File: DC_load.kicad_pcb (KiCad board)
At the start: 2 copper layers, 110 x 145 mm, 103 parts, among them J1 Conn_Coaxial, J2 red_terminal, J3 4 mm terminal, J4 4 mm terminal, J5 black terminal, J6 USB_B, Q3 FQP19N20C, Q4 FQP19N20C, Q5 FQP19N20C, Q6 FQP19N20C, SW1 RotaryEncoder_Switch, SW2 RotaryEncoder_Switch, U1 FSA3157P6X, U10 FSA3157P6X, U11 FSA3157P6X, U12 FSA3157P6X, U14 AMS1117-3.3, U15 74HC14D653, U16 LM4040DBZ-3, U2 Screen, U3 NCS21802, U4 NCS21802, U5 TLV9062, U6 TLV9062, U7 LMT84LPM, U8 STM32F103C8Tx, U9 CH340C

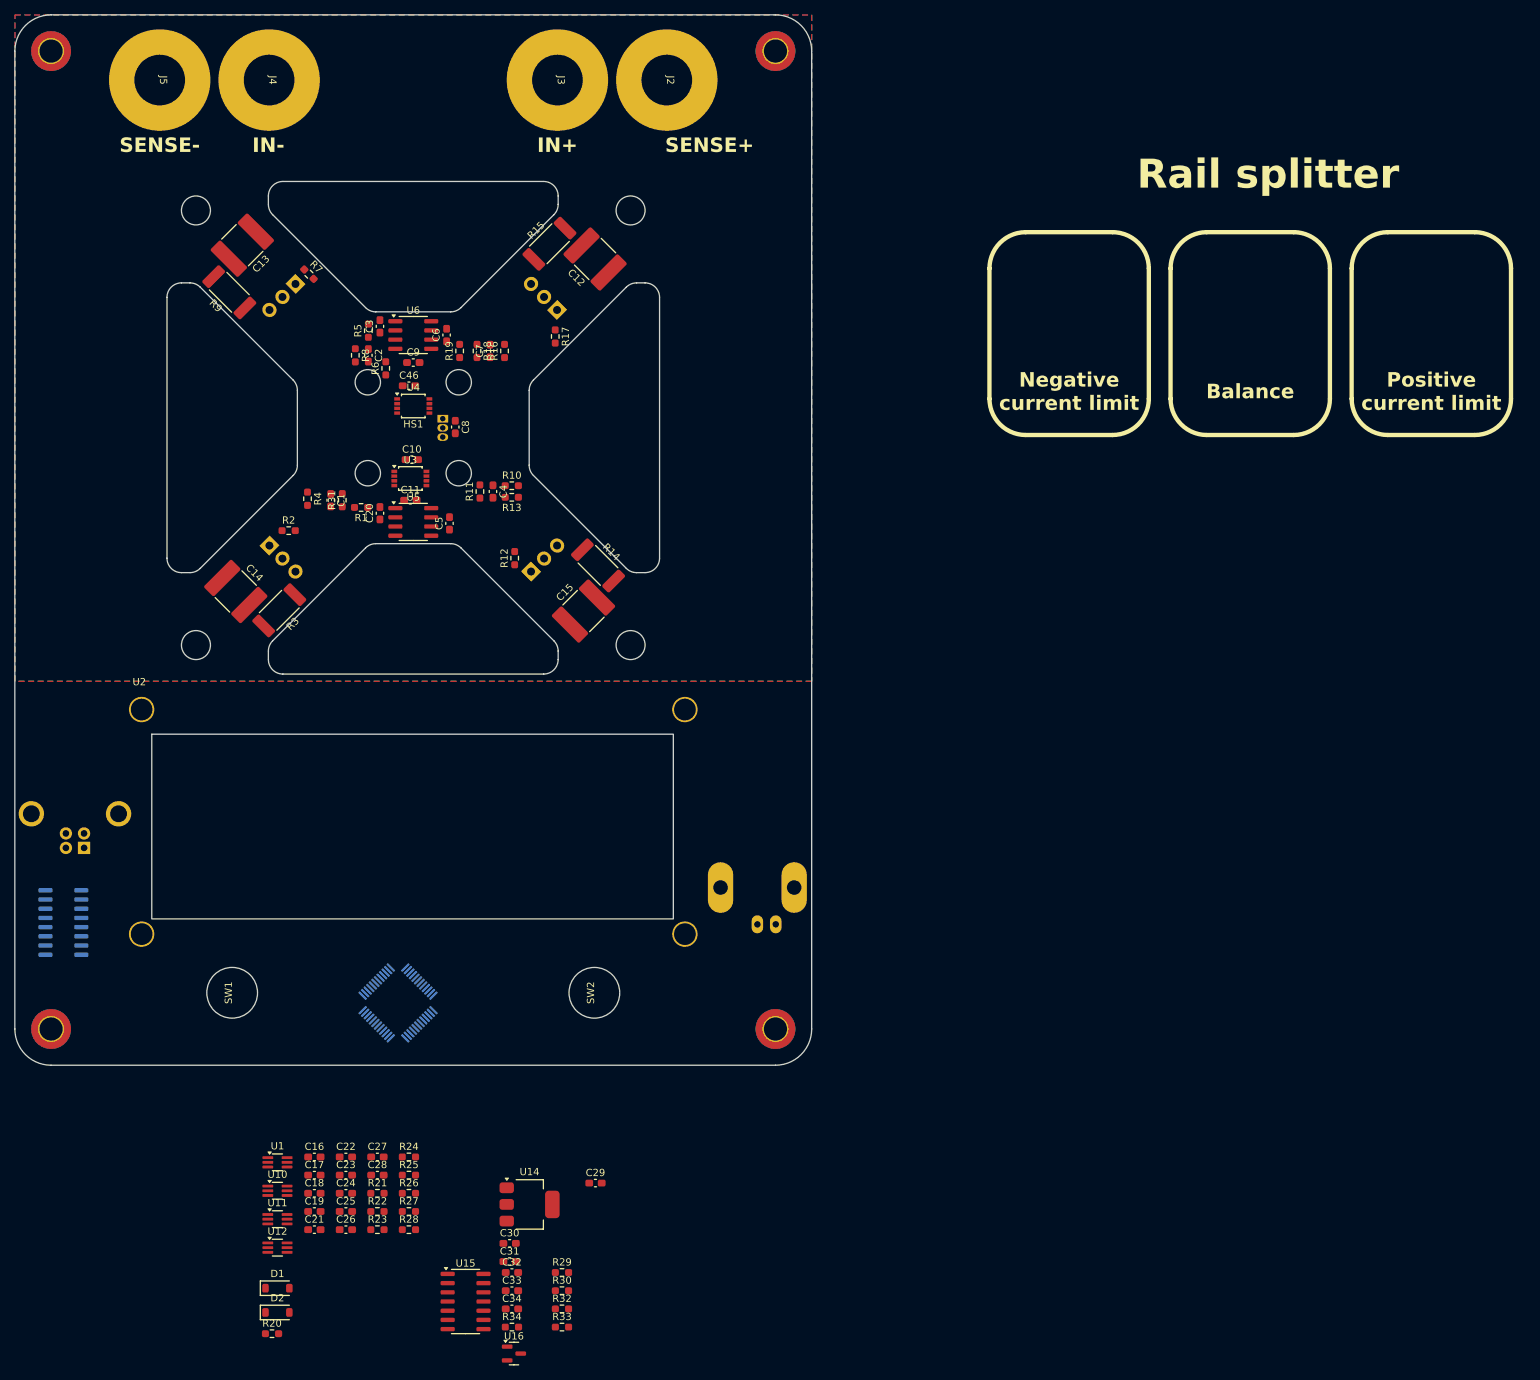
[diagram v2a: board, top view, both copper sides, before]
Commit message: Schematic and placement update.
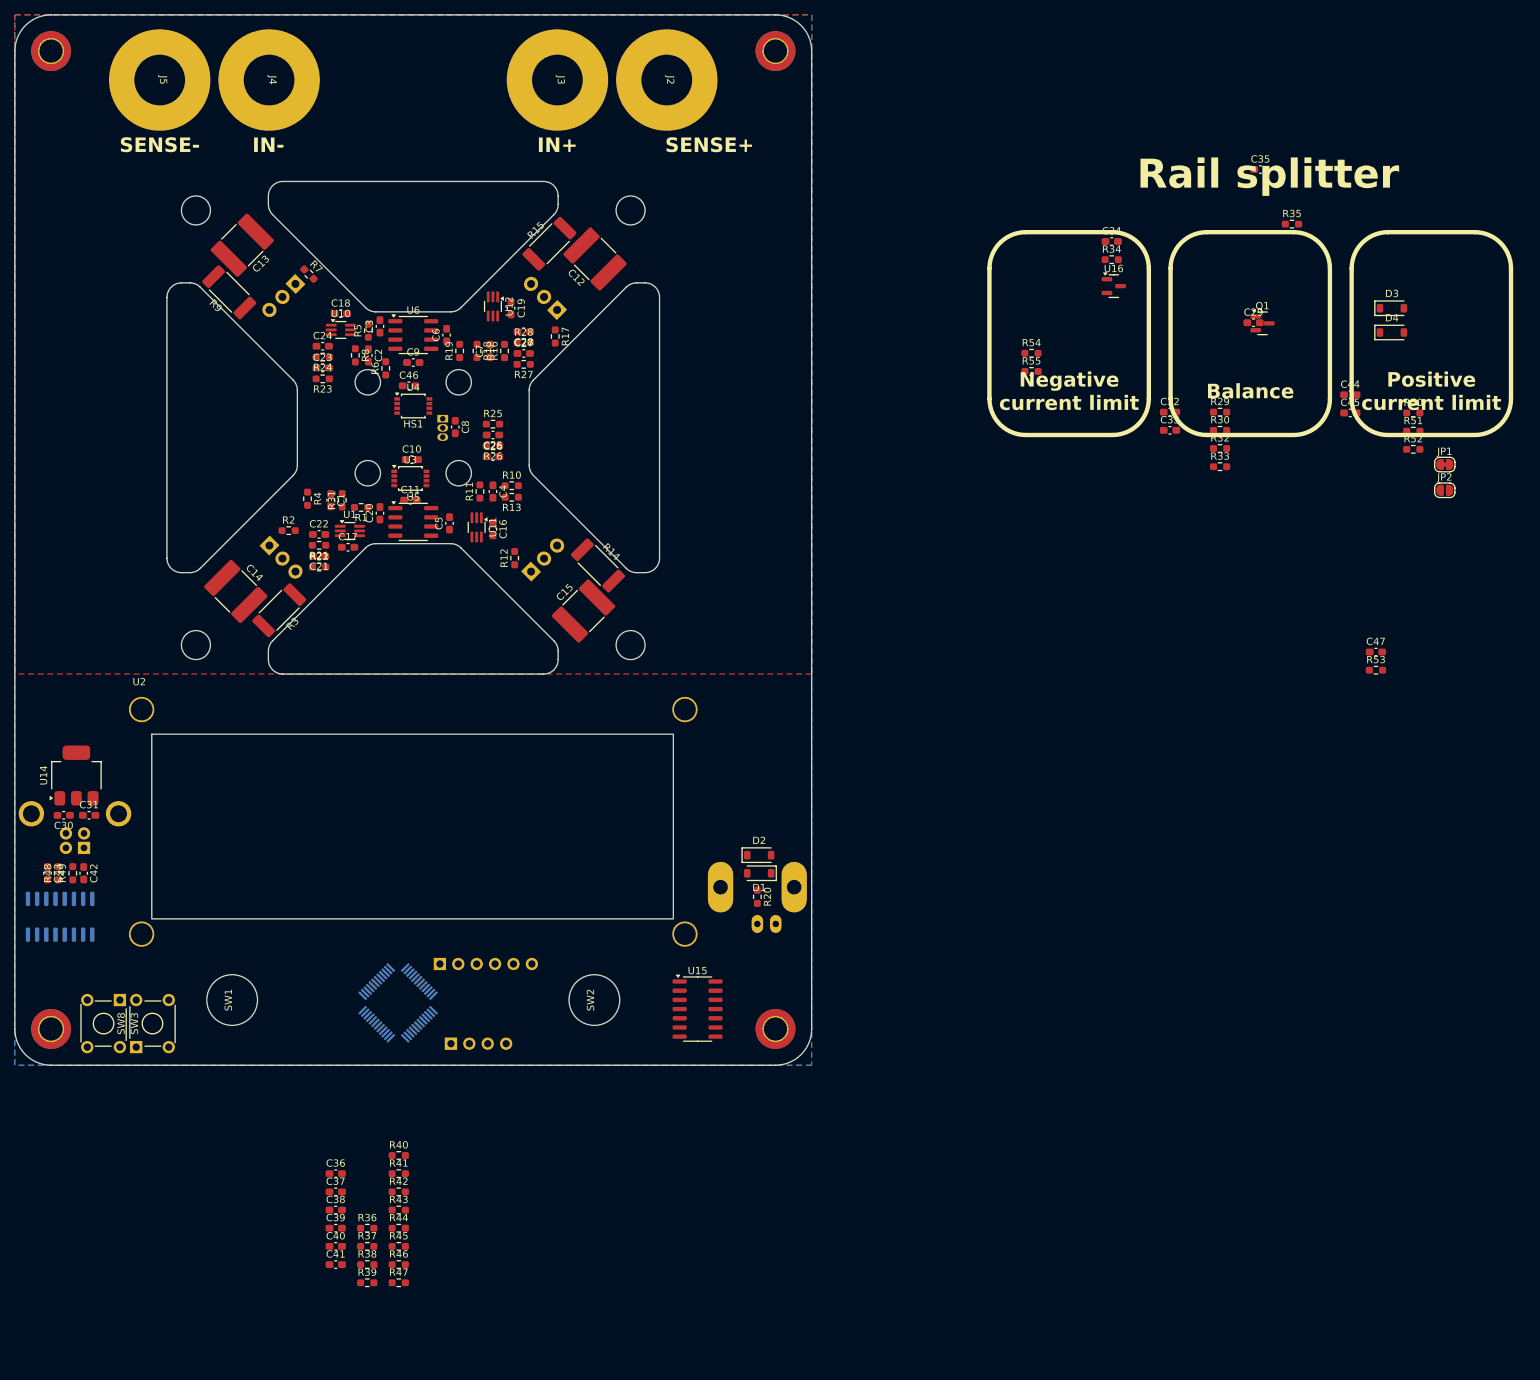
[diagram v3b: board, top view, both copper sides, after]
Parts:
- removed U9: CH340C, Package_SO:SOIC-16_3.9x9.9mm_P1.27mm
- added C35: 10u, Capacitor_SMD:C_0603_1608Metric_Pad1.08x0.95mm_HandSolder, F.Cu at (222.0, 71.4)
- added C36: 100n, Capacitor_SMD:C_0603_1608Metric_Pad1.08x0.95mm_HandSolder, F.Cu at (94.3, 210.0)
- added C37: 10n, Capacitor_SMD:C_0603_1608Metric_Pad1.08x0.95mm_HandSolder, F.Cu at (94.3, 212.5)
- added C38: 10n, Capacitor_SMD:C_0603_1608Metric_Pad1.08x0.95mm_HandSolder, F.Cu at (94.3, 215.0)
- added C39: 100n, Capacitor_SMD:C_0603_1608Metric_Pad1.08x0.95mm_HandSolder, F.Cu at (94.3, 217.5)
- added C40: 10n, Capacitor_SMD:C_0603_1608Metric_Pad1.08x0.95mm_HandSolder, F.Cu at (94.3, 220.0)
- added C41: 10n, Capacitor_SMD:C_0603_1608Metric_Pad1.08x0.95mm_HandSolder, F.Cu at (94.3, 222.5)
- added C42: 47p, Capacitor_SMD:C_0603_1608Metric_Pad1.08x0.95mm_HandSolder, F.Cu at (59.5, 168.5)
- added C43: 47p, Capacitor_SMD:C_0603_1608Metric_Pad1.08x0.95mm_HandSolder, F.Cu at (54.5, 168.5)
- added C44: 10n, Capacitor_SMD:C_0603_1608Metric_Pad1.08x0.95mm_HandSolder, F.Cu at (234.3, 102.5)
- added C45: 100n, Capacitor_SMD:C_0603_1608Metric_Pad1.08x0.95mm_HandSolder, F.Cu at (234.3, 105.0)
- added C47: 100n, Capacitor_SMD:C_0603_1608Metric_Pad1.08x0.95mm_HandSolder, F.Cu at (237.9, 138.0)
- added D3: 1N4148W, Diode_SMD:D_SOD-123, F.Cu at (240.1, 90.5)
- added D4: 1N4148W, Diode_SMD:D_SOD-123, F.Cu at (240.1, 93.8)
- added J7: Conn_01x06_Socket, Connector_PinSocket_2.54mm:PinSocket_1x06_P2.54mm_Vertical, B.Cu at (108.7, 181.0)
- added J9: Conn_01x04_Socket, Connector_PinSocket_2.54mm:PinSocket_1x04_P2.54mm_Vertical, B.Cu at (110.2, 192.0)
- added JP1: Jumper_2_Bridged, Jumper:SolderJumper-2_P1.3mm_Bridged_RoundedPad1.0x1.5mm, F.Cu at (247.4, 112.1)
- added JP2: Jumper_2_Open, Jumper:SolderJumper-2_P1.3mm_Open_RoundedPad1.0x1.5mm, F.Cu at (247.4, 115.6)
- added Q1: MMBT5401, Package_TO_SOT_SMD:SOT-23, F.Cu at (222.2, 92.6)
- added R35: 100, Resistor_SMD:R_0603_1608Metric_Pad0.98x0.95mm_HandSolder, F.Cu at (226.3, 78.9)
- added R36: 10k, Resistor_SMD:R_0603_1608Metric_Pad0.98x0.95mm_HandSolder, F.Cu at (98.7, 217.5)
- added R37: 10k, Resistor_SMD:R_0603_1608Metric_Pad0.98x0.95mm_HandSolder, F.Cu at (98.7, 220.0)
- added R38: 100k, Resistor_SMD:R_0603_1608Metric_Pad0.98x0.95mm_HandSolder, F.Cu at (98.7, 222.5)
- added R39: 10k, Resistor_SMD:R_0603_1608Metric_Pad0.98x0.95mm_HandSolder, F.Cu at (98.7, 225.0)
- added R40: 100k, Resistor_SMD:R_0603_1608Metric_Pad0.98x0.95mm_HandSolder, F.Cu at (103.0, 207.5)
- added R41: 10k, Resistor_SMD:R_0603_1608Metric_Pad0.98x0.95mm_HandSolder, F.Cu at (103.0, 210.0)
- added R42: 100k, Resistor_SMD:R_0603_1608Metric_Pad0.98x0.95mm_HandSolder, F.Cu at (103.0, 212.5)
- added R43: 10k, Resistor_SMD:R_0603_1608Metric_Pad0.98x0.95mm_HandSolder, F.Cu at (103.0, 215.0)
- added R44: 100k, Resistor_SMD:R_0603_1608Metric_Pad0.98x0.95mm_HandSolder, F.Cu at (103.0, 217.5)
- added R45: 10k, Resistor_SMD:R_0603_1608Metric_Pad0.98x0.95mm_HandSolder, F.Cu at (103.0, 220.0)
- added R46: 100k, Resistor_SMD:R_0603_1608Metric_Pad0.98x0.95mm_HandSolder, F.Cu at (103.0, 222.5)
- added R47: 100k, Resistor_SMD:R_0603_1608Metric_Pad0.98x0.95mm_HandSolder, F.Cu at (103.0, 225.0)
- added R48: 22, Resistor_SMD:R_0603_1608Metric_Pad0.98x0.95mm_HandSolder, F.Cu at (56.0, 168.5)
- added R49: 22, Resistor_SMD:R_0603_1608Metric_Pad0.98x0.95mm_HandSolder, F.Cu at (58.0, 168.5)
- added R50: 100, Resistor_SMD:R_0603_1608Metric_Pad0.98x0.95mm_HandSolder, F.Cu at (243.1, 105.0)
- added R51: 10k, Resistor_SMD:R_0603_1608Metric_Pad0.98x0.95mm_HandSolder, F.Cu at (243.1, 107.5)
- added R52: 100, Resistor_SMD:R_0603_1608Metric_Pad0.98x0.95mm_HandSolder, F.Cu at (243.1, 110.0)
- added R53: 10k, Resistor_SMD:R_0603_1608Metric_Pad0.98x0.95mm_HandSolder, F.Cu at (237.9, 140.5)
- added R54: 10k, Resistor_SMD:R_0603_1608Metric_Pad0.98x0.95mm_HandSolder, F.Cu at (190.3, 96.7)
- added R55: 10k, Resistor_SMD:R_0603_1608Metric_Pad0.98x0.95mm_HandSolder, F.Cu at (190.3, 99.2)
- added SW3: SW_Push, Button_Switch_THT:SW_TH_Tactile_Omron_B3F-10xx, F.Cu at (64.5, 186.0)
- added SW8: SW_Push, Button_Switch_THT:SW_TH_Tactile_Omron_B3F-10xx, F.Cu at (66.8, 192.5)
- added U17: CH340C, Package_SO:SOIC-16_3.9x9.9mm_P1.27mm, B.Cu at (56.2, 174.5)
- J3: value 4 mm terminal -> red terminal
- J4: value 4 mm terminal -> black terminal
- moved R34 169.0 mm to (201.4, 83.8)
- moved U16 169.0 mm to (201.7, 87.5)
- moved C34 169.0 mm to (201.4, 81.3)
- moved C29 149.5 mm to (221.0, 92.5)
- moved C32 149.5 mm to (209.5, 104.8)
- moved R29 149.5 mm to (216.4, 104.8)
- moved R33 149.5 mm to (216.4, 112.4)
- moved C33 149.5 mm to (209.5, 107.4)
- moved R30 149.5 mm to (216.4, 107.4)
- moved R32 149.5 mm to (216.4, 109.9)
- moved U12 133.3 mm to (116.0, 90.2), turned to -90 degrees
- moved C19 127.6 mm to (118.5, 90.5), turned to -90 degrees
- moved R28 123.5 mm to (120.2, 95.2)
- moved C18 121.5 mm to (95.0, 91.2)
- moved U10 119.2 mm to (95.0, 93.5)
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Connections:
- net CH1_MCU_CONTROL renamed Net-(C22-Pad2)
- net CH2_MCU_CONTROL renamed Net-(C24-Pad2)
- net CH3_MCU_CONTROL renamed Net-(C26-Pad2)
- net CH4_MCU_CONTROL renamed Net-(C28-Pad2)
- net V_SENSE+ renamed /Power_stage/V_SENSE+
- net V_SENSE- renamed /Power_stage/V_SENSE-
- C2 pad 1: CH2_MEAS -> /Microcontroller/CH2_MEAS
- C20 pad 1: CH1_MEAS -> /Microcontroller/CH1_MEAS
- C32 pad 2: VREF -> Net-(JP1-A)
- C5 pad 1: CH3_MEAS -> /Microcontroller/CH3_MEAS
- C7 pad 1: CH4_MEAS -> /Microcontroller/CH4_MEAS
- D1 pad 1: BNC_CONTROL -> /Microcontroller/BNC_CONTROL
- D2 pad 2: BNC_CONTROL -> /Microcontroller/BNC_CONTROL
- R10 pad 2: CH3_MEAS -> /Microcontroller/CH3_MEAS
- R18 pad 2: CH4_MEAS -> /Microcontroller/CH4_MEAS
- R19 pad 1: CH4_MEAS -> /Microcontroller/CH4_MEAS
- R20 pad 1: Net-(J1-In) -> /Microcontroller/BNC_CONTROL
- R20 pad 2: BNC_CONTROL -> Net-(J1-In)
- R4 pad 2: CH1_MEAS -> /Microcontroller/CH1_MEAS
- R5 pad 1: CH2_MEAS -> /Microcontroller/CH2_MEAS
- R6 pad 2: CH2_MEAS -> /Microcontroller/CH2_MEAS
- U1 pad 1: BNC_CONTROL -> /Microcontroller/BNC_CONTROL
- U1 pad 6: CH1_SEL -> CTRL_SEL
- U10 pad 1: BNC_CONTROL -> /Microcontroller/BNC_CONTROL
- U10 pad 6: CH2_SEL -> CTRL_SEL
- U11 pad 1: BNC_CONTROL -> /Microcontroller/BNC_CONTROL
- U11 pad 6: CH3_SEL -> CTRL_SEL
- U12 pad 1: BNC_CONTROL -> /Microcontroller/BNC_CONTROL
- U12 pad 6: CH4_SEL -> CTRL_SEL
- U15 pad 14: VREF -> Net-(JP1-A)
- U4 pad 1: CH2_MEAS -> /Microcontroller/CH2_MEAS
- U4 pad 7: CH4_MEAS -> /Microcontroller/CH4_MEAS
- U5 pad 2: CH1_MEAS -> /Microcontroller/CH1_MEAS
- U5 pad 6: CH3_MEAS -> /Microcontroller/CH3_MEAS
- U8 pad 1: unconnected-(U8-VBAT-Pad1) -> 3V3
- U8 pad 10: unconnected-(U8-PA0-Pad10) -> /Microcontroller/CH1_MEAS
- U8 pad 11: unconnected-(U8-PA1-Pad11) -> /Microcontroller/CH2_MEAS
- U8 pad 12: unconnected-(U8-PA2-Pad12) -> /Microcontroller/TX2
- U8 pad 13: unconnected-(U8-PA3-Pad13) -> TX
- U8 pad 14: unconnected-(U8-PA4-Pad14) -> /Microcontroller/CH3_MEAS
- U8 pad 16: unconnected-(U8-PA6-Pad16) -> CH3_PWM
- U8 pad 17: unconnected-(U8-PA7-Pad17) -> CH4_PWM
- U8 pad 18: unconnected-(U8-PB0-Pad18) -> /Microcontroller/CH4_MEAS
- U8 pad 23: Net-(U8-VSS-Pad23) -> GND
- U8 pad 29: unconnected-(U8-PA8-Pad29) -> CH1_PWM
- U8 pad 30: unconnected-(U8-PA9-Pad30) -> RX
- U8 pad 31: unconnected-(U8-PA10-Pad31) -> TX
- U8 pad 35: Net-(U8-VSS-Pad23) -> GND
- U8 pad 38: unconnected-(U8-PA15-Pad38) -> CH2_PWM
- U8 pad 42: unconnected-(U8-PB6-Pad42) -> SCL
- U8 pad 43: unconnected-(U8-PB7-Pad43) -> SDA
- U8 pad 44: unconnected-(U8-BOOT0-Pad44) -> BOOT
- U8 pad 47: Net-(U8-VSS-Pad23) -> GND
- U8 pad 7: unconnected-(U8-NRST-Pad7) -> RESET
- U8 pad 8: unconnected-(U8-VSSA-Pad8) -> GND
